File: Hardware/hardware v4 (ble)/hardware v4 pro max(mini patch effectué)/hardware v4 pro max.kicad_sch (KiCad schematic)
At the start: 50 parts, among them IC1 MLPF-WB-01E3, IC2 W25Q128JVPIQ_TR, J3 OLED, J4 USB_C_Receptacle_USB2.0_14P, SW4 boot, SW5 RSTBTN, U1 STM32WB55CGUx, U4 USBLC6-2SC6, Y1 Crystal_GND24

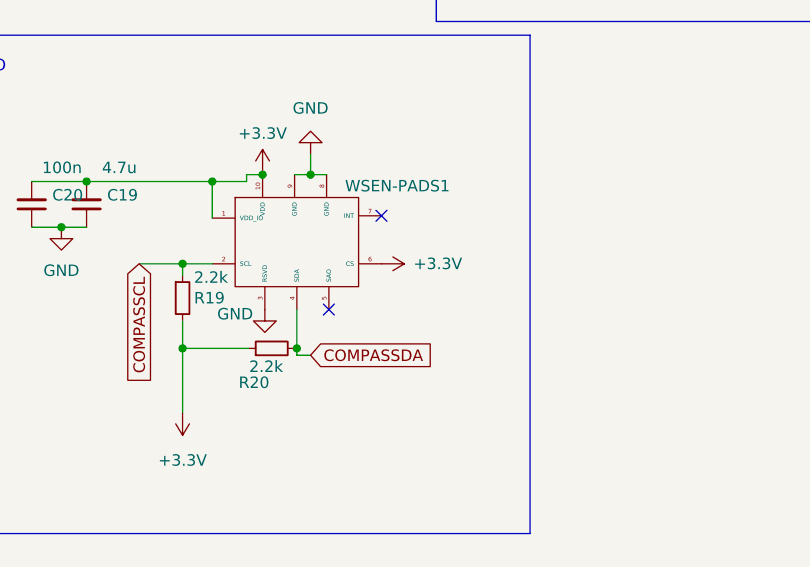
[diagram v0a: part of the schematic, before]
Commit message: board v5 gps 25Hz !!
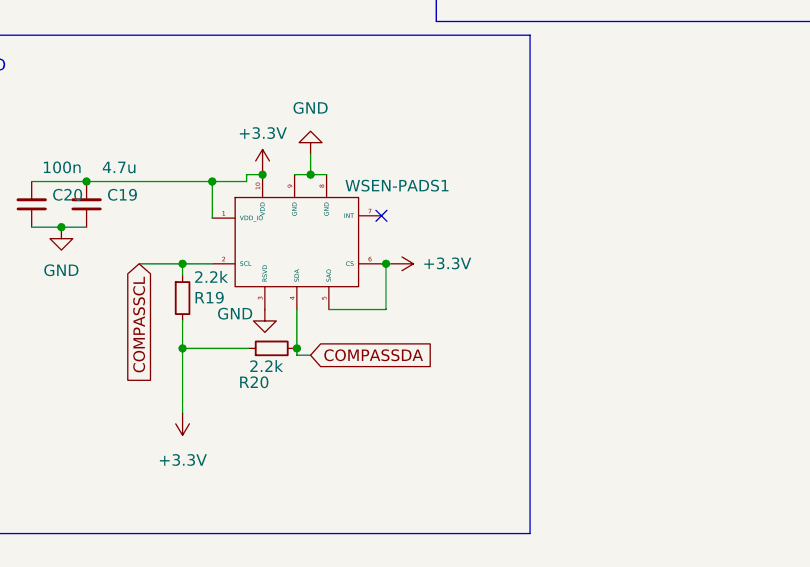
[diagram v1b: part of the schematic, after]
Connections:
- net +3.3V: now also WSEN-PADS1.5 (SAO)
- no-connect marks 16 -> 15
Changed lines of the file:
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@@
 	)
 	(junction
+		(at 147.828 185.42)
+		(diameter 0)
+		(color 0 0 0 0)
+	)
+	(junction
 		(at 91.44 104.14)
 		(diameter 0)
@@
 	)
 	(no_connect
-		(at 141.478 190.5)
-	)
-	(no_connect
 		(at 49.53 130.81)
 	)
@@
 	(wire
 		(pts
+			(xy 147.828 185.42) (xy 147.32 185.42)
+		)
+		(stroke
+			(width 0)
+			(type default)
+		)
+	)
+	(wire
+		(pts
 			(xy 81.28 133.35) (xy 90.17 133.35)
 		)
@@
 	(wire
 		(pts
+			(xy 148.336 185.42) (xy 147.828 185.42)
+		)
+		(stroke
+			(width 0)
+			(type default)
+		)
+	)
+	(wire
+		(pts
 			(xy 254 99.06) (xy 254 95.504)
 		)
@@
 	(wire
 		(pts
+			(xy 141.478 190.5) (xy 147.828 190.5)
+		)
+		(stroke
+			(width 0)
+			(type default)
+		)
+	)
+	(wire
+		(pts
 			(xy 281.94 65.786) (xy 281.94 67.564)
 		)
@@
 	(wire
 		(pts
+			(xy 147.828 190.5) (xy 147.828 185.42)
+		)
+		(stroke
+			(width 0)
+			(type default)
+		)
+	)
+	(wire
+		(pts
 			(xy 311.912 115.57) (xy 320.802 115.57)
 		)
@@
 	(symbol
 		(lib_id "power:+3.3V")
-		(at 147.32 185.42 270)
+		(at 148.336 185.42 270)
 		(unit 1)
 		(exclude_from_sim no)
@@
 		(fields_autoplaced yes)
 		(property "Reference" "#PWR048"
-			(at 143.51 185.42 0)
+			(at 144.526 185.42 0)
 			(effects
 				(font
@@
 		)
 		(property "Value" "+3.3V"
-			(at 150.876 185.4199 90)
+			(at 151.892 185.4199 90)
 			(effects
 				(font
@@
 		)
 		(property "Footprint" ""
-			(at 147.32 185.42 0)
+			(at 148.336 185.42 0)
 			(effects
 				(font
@@
 		)
 		(property "Datasheet" ""
-			(at 147.32 185.42 0)
+			(at 148.336 185.42 0)
 			(effects
 				(font
@@
 		)
 		(property "Description" "Power symbol creates a global label with name \"+3.3V\""
-			(at 147.32 185.42 0)
+			(at 148.336 185.42 0)
 			(effects
 				(font

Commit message: yhry
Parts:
- ANT1: footprint 74889302450(antenne):74889302450 -> antennesmd:74889302450
- J4: footprint USBWURTH:USBC-WURTH -> USBCWURTH:USB4110_USBC_SMT
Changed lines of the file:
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@@
 			)
 		)
-		(property "Footprint" "USBWURTH:USBC-WURTH"
+		(property "Footprint" "USBCWURTH:USB4110_USBC_SMT"
 			(at 47.244 193.04 0)
 			(effects
@@
 			)
 		)
-		(property "Footprint" "74889302450(antenne):74889302450"
+		(property "Footprint" "antennesmd:74889302450"
 			(at 97.358 151.384 0)
 			(effects
